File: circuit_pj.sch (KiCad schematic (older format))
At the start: 38 parts, among them J1 PWR, J2 Comm, J3 Drive_pin, J4 9V, Q1 2N3904, Q2 2N3904, Q3 2N3906, Q4 2N3904, Q5 2N3906, SW1 PWR_S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

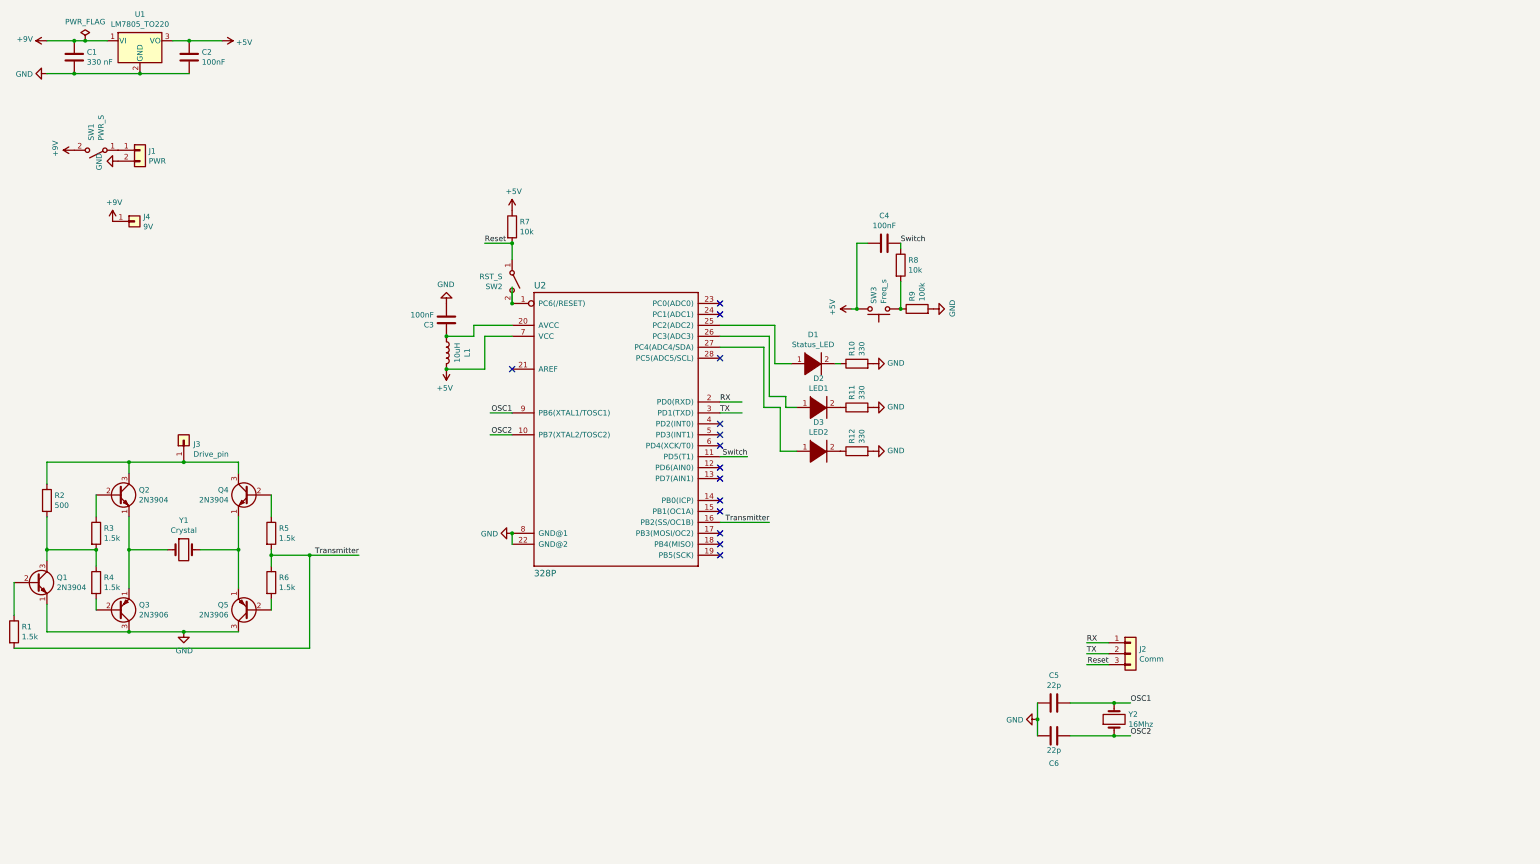
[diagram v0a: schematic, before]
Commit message: changed reset pin from a switch to a jumper, also reorganized the schematic
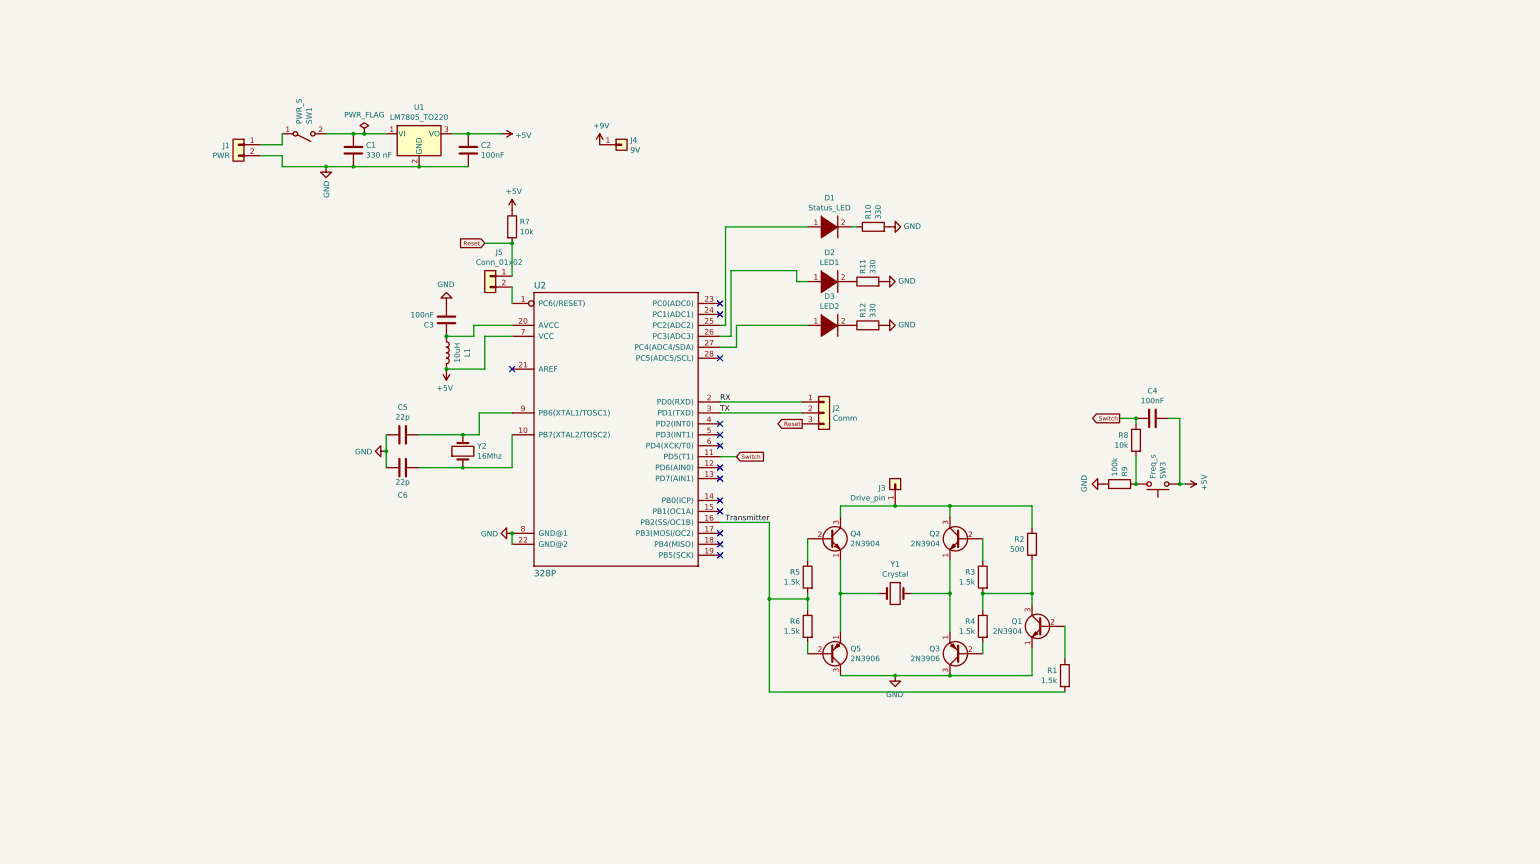
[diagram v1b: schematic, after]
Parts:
- removed SW2: RST_S, Button_Switch_THT:SW_DIP_SPSTx01_Slide_6.7x4.1mm_W7.62mm_P2.54mm_LowProfile, symbol Switch:SW_SPST
- added J5: Conn_01x02, Connector_PinHeader_2.54mm:PinHeader_1x02_P2.54mm_Vertical, symbol Connector_Generic:Conn_01x02
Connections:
- net labels removed: OSC1, OSC2
- wire segments 83 -> 85
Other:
- moved on the sheet: C1, C2, C4, C5, C6, D1, D2, D3, J1, J2, J3, J4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

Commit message: adjusted sch and pcb after ltspice simulation, switched PNP and NPN positions and also connected the piezo to the collector pins instead of the emitters.
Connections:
- net GND: now also Q2.1 (E), Q4.1 (E); no longer Q3.3 (C), Q5.3 (C)
- net at Q3.2 (B): now also R3.1; no longer R4.2
- net at Q5.2 (B): now also R5.1; no longer R6.2
- net at Q2.2 (B): now also R4.2; no longer R3.1
- net at J3.1 (Pin_1), R2.1: now also Q3.1 (E), Q5.1 (E); no longer Q2.3 (C), Q4.3 (C)
- net at Q4.2 (B): now also R6.2; no longer R5.1
- new net: Q2.3 (C), Q3.3 (C), Y1.1
- new net: Q4.3 (C), Q5.3 (C), Y1.2
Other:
- note added: "The H-bridge inverter will always draw current, make sure to add an external switch to the pin to avoid that from happening"
- moved on the sheet: Q2, Q3, Q4, Q5
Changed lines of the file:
@@
 L Transistor_BJT:2N3906 Q3
 U 1 1 5EC7C800
-P 8950 6250
-F 0 "Q3" H 9141 6204 50  0000 L CNN
-F 1 "2N3906" H 9141 6295 50  0000 L CNN
-F 2 "Package_TO_SOT_THT:TO-92_Inline" H 9150 6175 50  0001 L CIN
-F 3 "https://www.fairchildsemi.com/datasheets/2N/2N3906.pdf" H 8950 6250 50  0001 L CNN
-	1    8950 6250
+P 8950 5200
+F 0 "Q3" H 9141 5154 50  0000 L CNN
+F 1 "2N3906" H 9141 5245 50  0000 L CNN
+F 2 "Package_TO_SOT_THT:TO-92_Inline" H 9150 5125 50  0001 L CIN
+F 3 "https://www.fairchildsemi.com/datasheets/2N/2N3906.pdf" H 8950 5200 50  0001 L CNN
+	1    8950 5200
 	-1   0    0    1
 $EndComp
@@
 L Transistor_BJT:2N3906 Q5
 U 1 1 5EC7DE02
-P 7750 6250
-F 0 "Q5" H 7941 6204 50  0000 L CNN
-F 1 "2N3906" H 7941 6295 50  0000 L CNN
-F 2 "Package_TO_SOT_THT:TO-92_Inline" H 7950 6175 50  0001 L CIN
-F 3 "https://www.fairchildsemi.com/datasheets/2N/2N3906.pdf" H 7750 6250 50  0001 L CNN
-	1    7750 6250
+P 7750 5200
+F 0 "Q5" H 7941 5154 50  0000 L CNN
+F 1 "2N3906" H 7941 5245 50  0000 L CNN
+F 2 "Package_TO_SOT_THT:TO-92_Inline" H 7950 5125 50  0001 L CIN
+F 3 "https://www.fairchildsemi.com/datasheets/2N/2N3906.pdf" H 7750 5200 50  0001 L CNN
+	1    7750 5200
 	1    0    0    1
 $EndComp
@@
 L Transistor_BJT:2N3904 Q2
 U 1 1 5EC7E557
-P 8950 5200
-F 0 "Q2" H 9140 5246 50  0000 L CNN
-F 1 "2N3904" H 9140 5155 50  0000 L CNN
-F 2 "Package_TO_SOT_THT:TO-92_Inline" H 9150 5125 50  0001 L CIN
-F 3 "https://www.fairchildsemi.com/datasheets/2N/2N3904.pdf" H 8950 5200 50  0001 L CNN
-	1    8950 5200
+P 8950 6250
+F 0 "Q2" H 9140 6296 50  0000 L CNN
+F 1 "2N3904" H 9140 6205 50  0000 L CNN
+F 2 "Package_TO_SOT_THT:TO-92_Inline" H 9150 6175 50  0001 L CIN
+F 3 "https://www.fairchildsemi.com/datasheets/2N/2N3904.pdf" H 8950 6250 50  0001 L CNN
+	1    8950 6250
 	-1   0    0    -1
 $EndComp
@@
 L Transistor_BJT:2N3904 Q4
 U 1 1 5EC9D472
-P 7750 5200
-F 0 "Q4" H 7940 5246 50  0000 L CNN
-F 1 "2N3904" H 7940 5155 50  0000 L CNN
-F 2 "Package_TO_SOT_THT:TO-92_Inline" H 7950 5125 50  0001 L CIN
-F 3 "https://www.fairchildsemi.com/datasheets/2N/2N3904.pdf" H 7750 5200 50  0001 L CNN
-	1    7750 5200
+P 7750 6250
+F 0 "Q4" H 7940 6296 50  0000 L CNN
+F 1 "2N3904" H 7940 6205 50  0000 L CNN
+F 2 "Package_TO_SOT_THT:TO-92_Inline" H 7950 6175 50  0001 L CIN
+F 3 "https://www.fairchildsemi.com/datasheets/2N/2N3904.pdf" H 7750 6250 50  0001 L CNN
+	1    7750 6250
 	1    0    0    -1
 $EndComp
@@
 Text GLabel 10400 4100 0    39   Output ~ 0
 Switch
+Text Notes 250  8050 0    118  ~ 0
+The H-bridge inverter will always draw current, make sure to add an external switch to the pin to avoid that from happening
 $EndSCHEMATC
